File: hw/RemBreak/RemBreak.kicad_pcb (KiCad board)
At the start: 2 copper layers, 40 x 80 mm, 79 parts, among them IC1 LTC2943IDD#TRPBF, J1 Screw_Terminal_01x04, J2 Screw_Terminal_01x04, J3 Screw_Terminal_01x02, J4 Conn_01x03_MountingPin, J5 Conn_02x06_Odd_Even, J6 Conn_01x07, J7 Conn_01x07, J8 Conn_01x03, Q1 BC337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

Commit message: added pin description silkscreen labels
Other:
- board text added: "5V 3V3"
- board text added: "DI DCKI"
- board text added: "GND RED"
- board text added: "GREEN BLUE"
- board text added: "ONOFF VBATT"
- board text added: "SCL SDA"
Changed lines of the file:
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@@
+		)
+	)
+	(gr_text "ONOFF\nVBATT"
+		(at 159 99 90)
+		(layer "B.SilkS")
+		(effects
+			(font
+				(size 0.7 0.7)
+				(thickness 0.1)
+			)
+			(justify left bottom mirror)
+		)
+	)
+	(gr_text "GREEN\nBLUE"
+		(at 159 109 90)
+		(layer "B.SilkS")
+		(effects
+			(font
+				(size 0.7 0.7)
+				(thickness 0.1)
+			)
+			(justify left bottom mirror)
+		)
+	)
+	(gr_text "SCL\nSDA"
+		(at 159 116 90)
+		(layer "B.SilkS")
+		(effects
+			(font
+				(size 0.7 0.7)
+				(thickness 0.1)
+			)
+			(justify left bottom mirror)
+		)
+	)
+	(gr_text "5V\n3V3"
+		(at 159 103 90)
+		(layer "B.SilkS")
+		(effects
+			(font
+				(size 0.7 0.7)
+				(thickness 0.1)
+			)
+			(justify left bottom mirror)
+		)
+	)
+	(gr_text "DI\nDCKI"
+		(at 159 113 90)
+		(layer "B.SilkS")
+		(effects
+			(font
+				(size 0.7 0.7)
+				(thickness 0.1)
+			)
+			(justify left bottom mirror)
+		)
+	)
+	(gr_text "GND\nRED"
+		(at 159 106 90)
+		(layer "B.SilkS")
+		(effects
+			(font
+				(size 0.7 0.7)
+				(thickness 0.1)
+			)
+			(justify left bottom mirror)
 		)
 	)

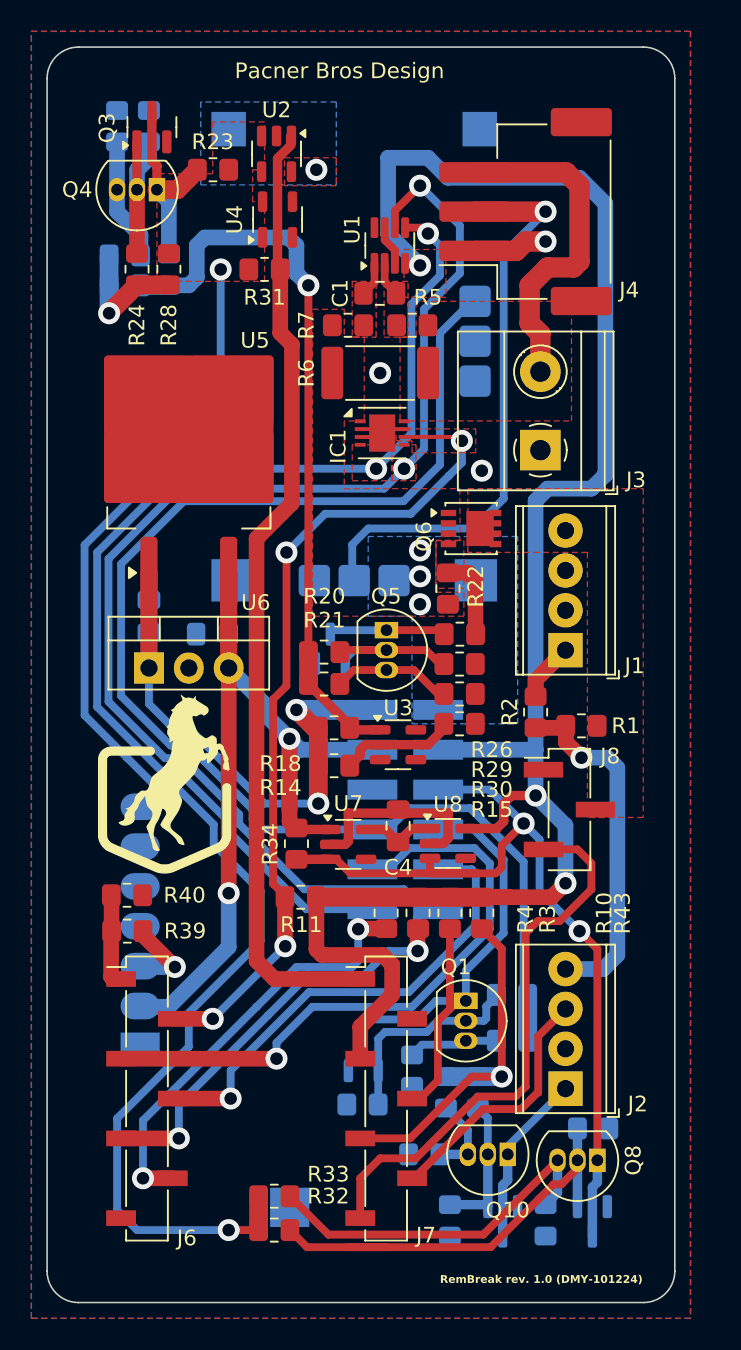
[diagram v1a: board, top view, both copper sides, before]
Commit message: rerouting in newer version of kicad
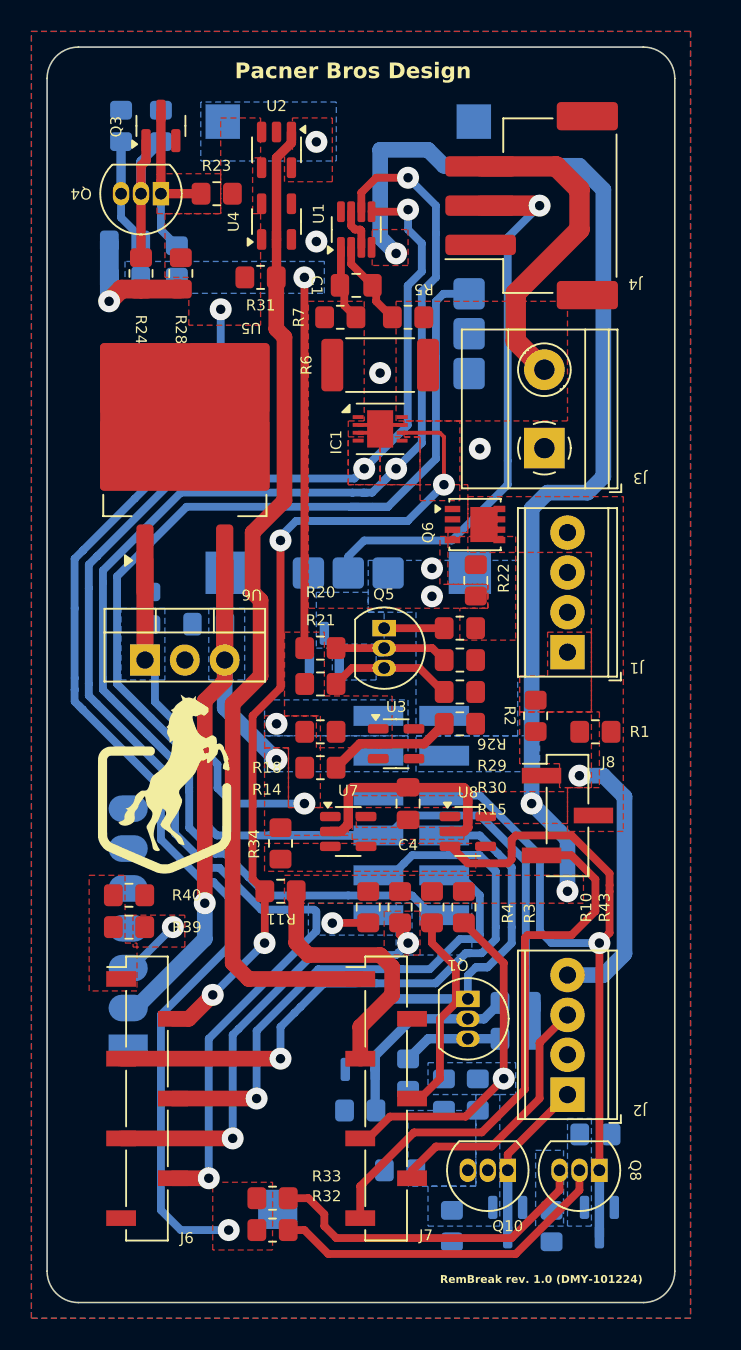
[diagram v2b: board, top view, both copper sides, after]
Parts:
- moved U1 2.37 mm to (139.7, 71.6)
- moved R22 1.85 mm to (147.3, 94.0)
- moved R42 1.84 mm to (142.5, 131.6)
- moved C1 1.59 mm to (139.7, 75.2)
- moved C4 1.55 mm to (143.0, 108.2)
- moved R23 1.54 mm to (130.8, 69.3)
- moved U8 1.49 mm to (146.8, 110.0)
- moved R11 1.34 mm to (134.9, 113.8)
- moved R10 1.20 mm to (144.5, 114.8)
- moved R3 1.20 mm to (142.5, 114.8)
- moved R4 1.20 mm to (140.5, 114.8)
- moved R43 1.20 mm to (146.6, 114.8)
- moved R34 1.02 mm to (134.9, 110.7)
- moved Q10 1.02 mm to (149.4, 131.6)
- moved R1 0.97 mm to (154.9, 103.6)
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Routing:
- net +3V3: track 116.0 -> 88.1 mm
- net Net-(U3-VOUT): track 46.8 -> 23.6 mm
- net +5V: track 57.7 -> 39.1 mm
- net /control_connector/ONOFF: track 35.6 -> 22.4 mm
- net /control_connector/LED GREEN: track 85.7 -> 97.7 mm
- net /power_manager/EN: track 85.0 -> 73.8 mm
- net Net-(Q10-B): track 9.01 -> 0.00 mm
- net /break_control/DISPLAY.DI: track 40.1 -> 47.7 mm
- net Net-(Q8-B): track 28.8 -> 22.1 mm
- net /break_control/RF SWITCH: track 5.92 -> 0.00 mm
- net Net-(Q6-G): track 5.40 -> 0.00 mm
- net Net-(Q10-E): track 5.31 -> 0.00 mm
- net Net-(J2-Pin_4): track 22.6 -> 17.6 mm
- net Net-(U7-VOUT): track 4.77 -> 0.00 mm
- net /break_control/BALARM: track 53.6 -> 57.9 mm
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- added copper zone on B.Cu, net +3V3
- added copper zone on B.Cu, net +5V
- added copper zone on F.Cu, net +5V
- added copper zone on B.Cu, net /break_control/BUZZ
- added copper zone on B.Cu, net /break_control/I2C.SCL
- added copper zone on B.Cu, net /break_control/I2C.SDA
- added copper zone on F.Cu, net /break_control/RF SWITCH
- added copper zone on F.Cu, net /control_connector/LED RED
- added copper zone on B.Cu, net /control_connector/ONOFF
- added copper zone on F.Cu, net /control_connector/ONOFF
- added copper zone on F.Cu, net Net-(J1-Pin_1)
- added copper zone on F.Cu, net Net-(J2-Pin_4)
- added copper zone on F.Cu, net Net-(M2-D0)
- added copper zone on B.Cu, net Net-(Q10-B)
- added copper zone on B.Cu, net Net-(Q10-E)
- added copper zone on F.Cu, net Net-(Q3-C)
- added copper zone on B.Cu, net Net-(Q5-B)
- added copper zone on B.Cu, net Net-(Q5-C)
- added copper zone on B.Cu, net Net-(Q8-B)
- added copper zone on B.Cu, net Net-(Q8-E)
- added copper zone on B.Cu, net Net-(U3-VOUT)
- added copper zone on F.Cu, net Net-(U3-VOUT)
- added copper zone on F.Cu, net Net-(U7-VOUT)
- removed copper zone on F.Cu, net Net-(U1-IN+)
- removed copper zone on F.Cu, net Net-(U1-IN-)

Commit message: DRC passed, ignored certain packages which have small pitches
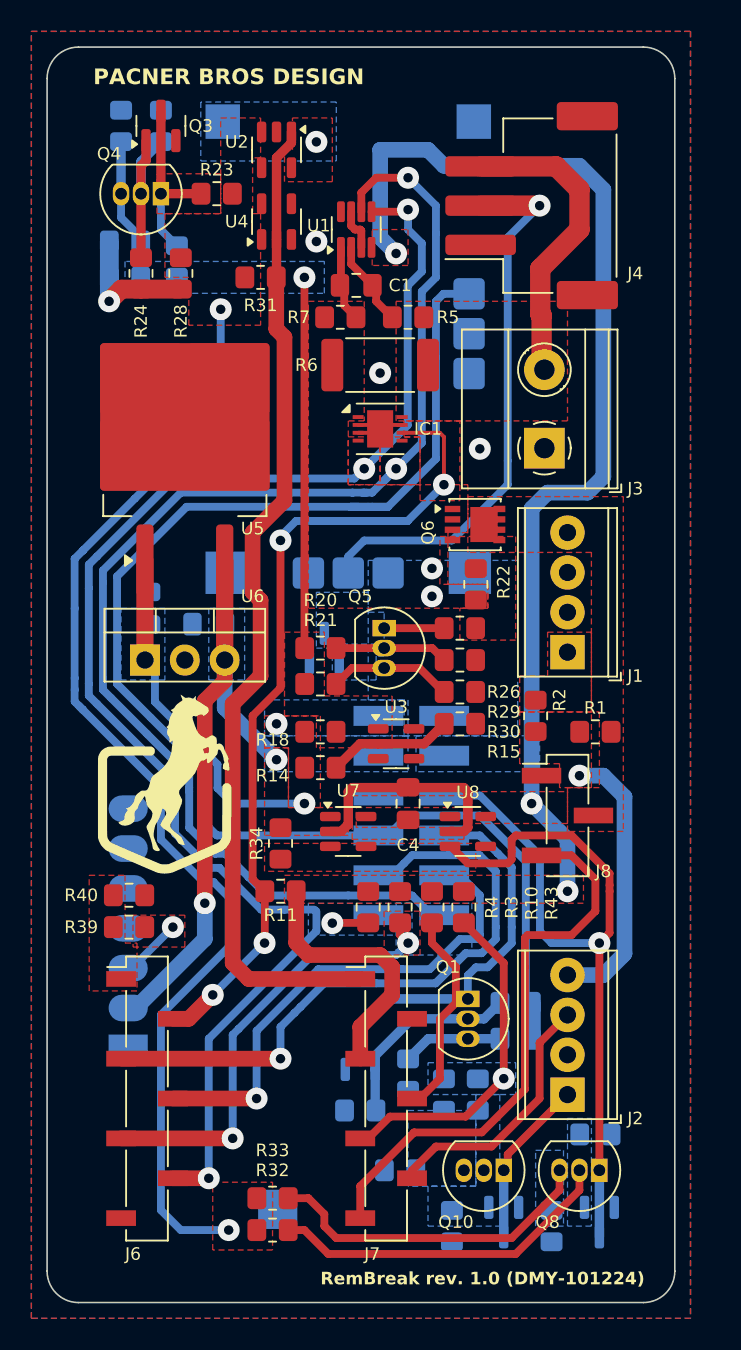
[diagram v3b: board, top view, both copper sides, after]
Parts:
- moved REF** 1.55 mm to (125.2, 87.9)
- moved REF** 1.52 mm to (125.2, 81.0)
- moved Q10 0.25 mm to (149.1, 131.6)
- moved Q11 0.25 mm to (149.1, 134.9)
- moved R22 0.25 mm to (147.3, 94.2)
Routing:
- net /control_connector/LED GREEN: track 97.7 -> 90.7 mm
- net /break_control/DISPLAY.DI: track 47.7 -> 45.4 mm
- net Net-(IC1-SENSE-): track 20.8 -> 19.5 mm
- net /control_connector/LED BLUE: track 38.5 -> 37.7 mm
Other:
- board text added: "7V5"
- board text added: "BATT+"
- board text added: "BATT-"
- board text added: "BTN"
- board text added: "EXTV"
- board text added: "GND"
- board text added: "GRN BLE"
- board text added: "PACNER BROS DESIGN"
- board text added: "SW BATT"
- board text added: "VBUZ"
- board text added: "VOUT"
- board text removed: "GREEN BLUE"
- board text removed: "ONOFF VBATT"
- board text removed: "Pacner Bros Design"

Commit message: first version and added jumper to connect buzz internally not just through handlebars
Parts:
- added JP1: SolderJumper_3_Open, Jumper:SolderJumper-3_P1.3mm_Open_RoundedPad1.0x1.5mm, B.Cu at (155.7, 121.7)
- moved R35 2.27 mm to (152.7, 129.3), turned to 0 degrees
- moved C4 0.51 mm to (143.0, 108.7)
- moved U7 0.51 mm to (139.2, 110.5)
- moved U8 0.51 mm to (146.8, 110.5)
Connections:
- R1 pad 2: Net-(J2-Pin_4) -> Net-(JP1-C)
- R2 pad 2: Net-(J2-Pin_4) -> Net-(JP1-C)
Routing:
- net Net-(JP1-C): track 0.00 -> 18.0 mm, vias 0 -> 1
- net Net-(J2-Pin_4): track 17.6 -> 0.00 mm, vias 1 -> 0
- net /break_control/SERVO: track 36.0 -> 33.8 mm
- added copper zone on B.Cu, net /break_control/BUZZER
- added copper zone on B.Cu, net Net-(J2-Pin_4)
- added copper zone on F.Cu, net Net-(JP1-C)
- removed copper zone on F.Cu, net Net-(J2-Pin_4)
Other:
- board text added: "BALANCE"
- board text added: "BATTERY"
- board text added: "EXT VOLTAGE"
- board text added: "HANDLEBARS"
- board text added: "SERVO"
